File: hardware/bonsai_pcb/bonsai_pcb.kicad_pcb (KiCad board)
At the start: 2 copper layers, 53 x 23 mm, 6 parts, among them J1 Audio Amp Conn, J3 PH2.0 Battery Connector, SW1 BT1, U1 XIAO-ESP32-S3-SMD

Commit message: Update PCB, schematic, and STEP model
Co-Authored-By: Claude Sonnet 5 <noreply@anthropic.com>
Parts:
- removed J1: Audio Amp Conn, Connector_PinSocket_2.54mm:PinSocket_1x07_P2.54mm_Vertical
- removed J3: PH2.0 Battery Connector, Connector_JST:JST_PH_S2B-PH-K_1x02_P2.00mm_Horizontal
- added +: Conn_01x01_Socket, Connector_Wire:SolderWirePad_1x01_SMD_2x4mm, F.Cu at (135.7, 99.0)
- added -: Conn_01x01_Socket, Connector_Wire:SolderWirePad_1x01_SMD_2x4mm, F.Cu at (135.7, 95.2)
- added C1: 10uF, JLCPCB_Capacitors:C0402, F.Cu at (143.0, 100.0)
- added C2: 100nF, JLCPCB_Capacitors:C0402, F.Cu at (143.0, 99.0)
- added CN2: S2B-PH-SM4-TB, JLCPCB_Connectors:CONN-SMD_P2.00_S2B-PH-SM4-TB-LF-SN, F.Cu at (168.8, 104.6)
- added M2: MountingHole_2.2mm_M2, MountingHole:MountingHole_2.2mm_M2, F.Cu at (170.9, 97.7)
- added U2: MAX98357AETE+T, JLCPCB_Amplifiers:TQFN-16_L3.0-W3.0-P0.50-BL-EP1.5, F.Cu at (141.8, 96.3)
- SW1: value BT1 -> TS-1102N-5516; footprint Button_Switch_THT:SW_PUSH_6mm -> JLCPCB_Switches:SW-TH_TS-1102N-5516
- moved SW1 30.2 mm to (138.0, 89.2), turned to 180 degrees
- moved J2 4.01 mm to (163.8, 104.7), turned to -155 degrees
- moved G*** 3.60 mm to (138.6, 94.1)
- renumbered B+ to J2
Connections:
- U1 pad 1: BT1 -> DIN
- U1 pad 10: BLCK -> SD
- U1 pad 2: unconnected-(U1-GPIO2_A1_D1-Pad2) -> BLCK
- U1 pad 3: unconnected-(U1-GPIO3_A2_D2-Pad3) -> LRC
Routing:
- net BLCK: track 28.7 -> 7.57 mm
- net LRC: track 25.8 -> 5.90 mm
- net BT1: track 21.5 -> 36.4 mm
- net /OUTP: track 0.00 -> 12.3 mm, vias 0 -> 2
- net /OUTN: track 0.00 -> 11.5 mm, vias 0 -> 2
- net DIN: track 0.00 -> 10.7 mm
- net GND: track 2.58 -> 12.1 mm, vias 17 -> 21
- net SD: track 37.0 -> 29.7 mm
- net Net-(J2-Pin_1): track 16.9 -> 9.70 mm, vias 0 -> 1
- net VIN: track 33.0 -> 31.1 mm
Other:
- board size 53 x 23 mm -> 41 x 23 mm
- board text removed: "⌈ ⌉ MAX98357 ⌊ ⌋"

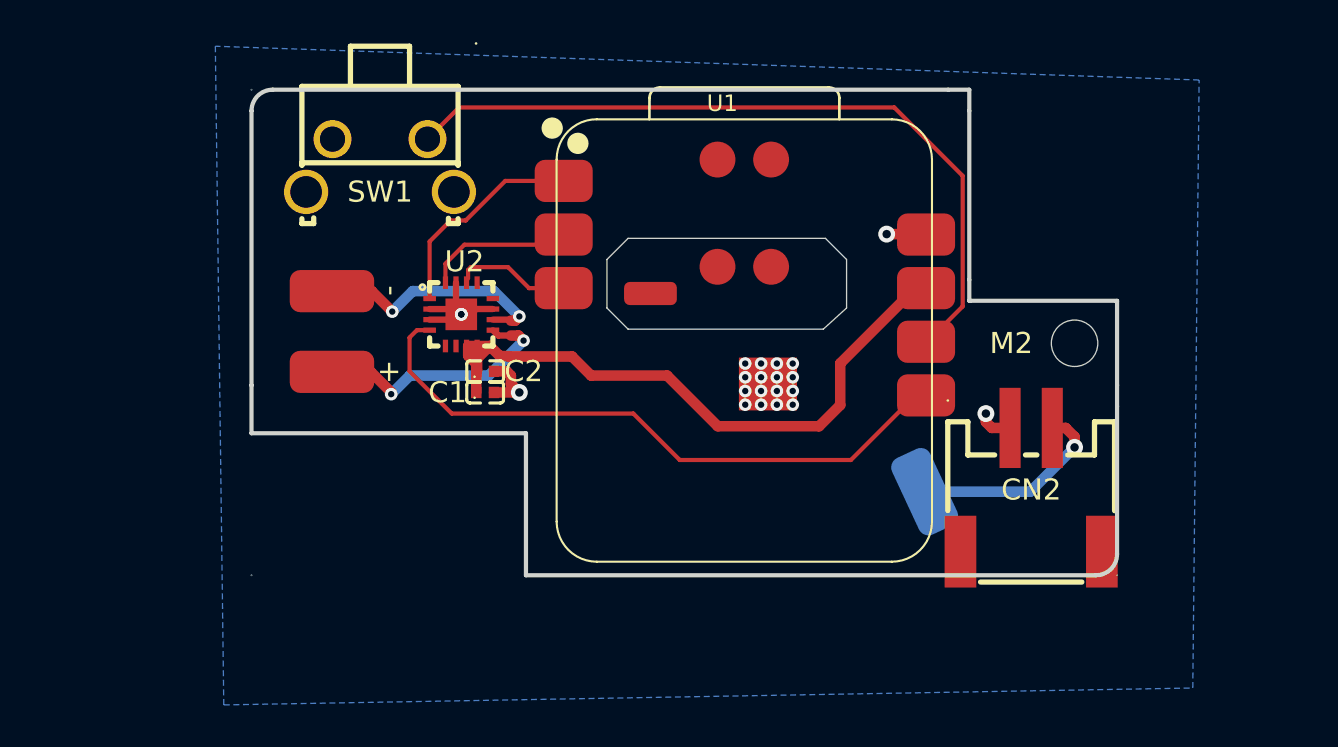
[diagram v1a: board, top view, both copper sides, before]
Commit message: Redraw the board with the tactile switch and the logo silkscreen
Brings in the JLCPCB tactile-switch symbol/footprint/3D model, adds the
logo footprint on the silkscreen, and reworks the schematic and layout
around them.

Co-Authored-By: Claude Opus 5 <noreply@anthropic.com>
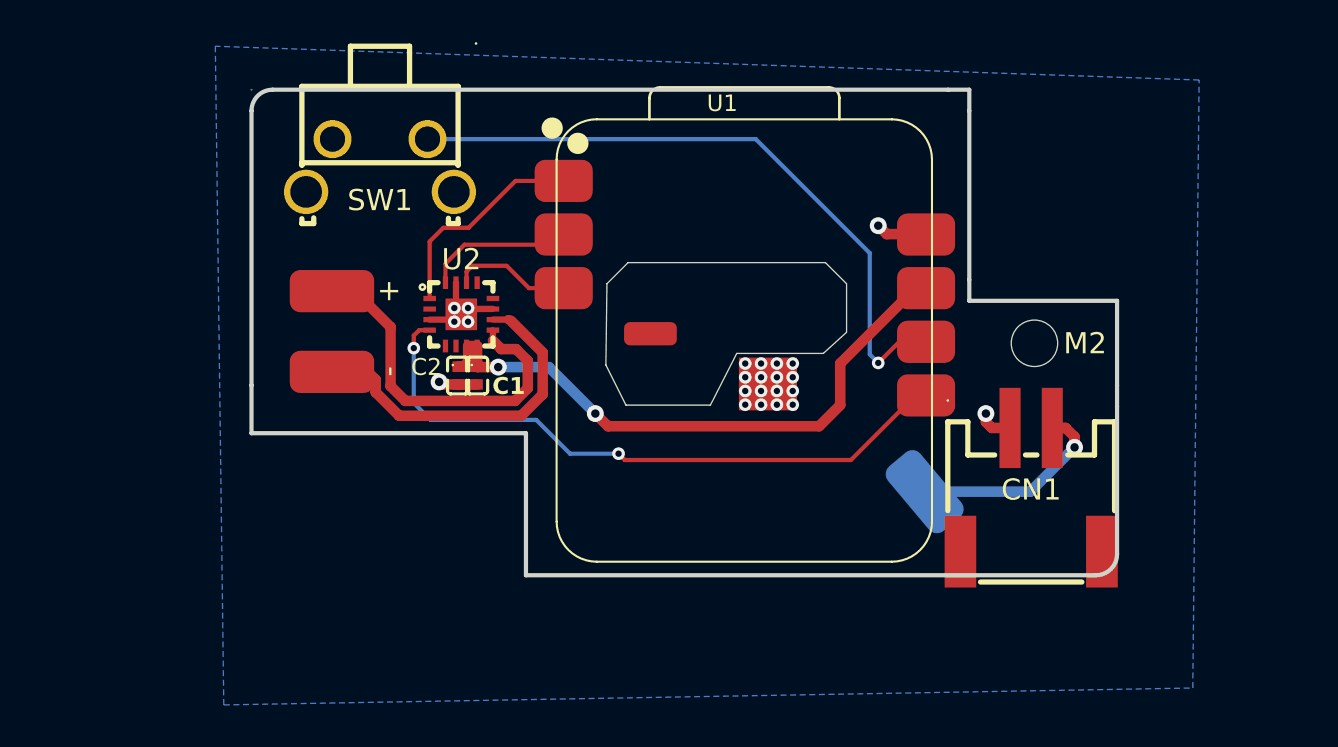
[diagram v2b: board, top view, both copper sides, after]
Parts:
- removed the G*** at (138.6, 94.1)
- added G***: LOGO, LOGO, B.Cu at (140.0, 94.0)
- J1: renamed from J2; value B+ Wire -> B+ Solder Pad
- moved + 3.83 mm to (135.7, 95.2)
- moved - 3.83 mm to (135.7, 99.0)
- moved M2 1.90 mm to (169.0, 97.7)
- moved C2 1.30 mm to (141.7, 99.2), turned to -90 degrees
- moved C1 0.89 mm to (142.6, 99.2), turned to -90 degrees
- turned J1 to 40 degrees
- renumbered CN2 to CN1
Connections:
- net Net-(J2-Pin_1) renamed /BAT +
- U2 pad 2: GND -> unconnected-(U2-GAIN_SLOT-Pad2)
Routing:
- net BT1: track 36.4 -> 30.7 mm, vias 0 -> 1
- net /OUTN: track 11.5 -> 16.7 mm, vias 2 -> 0
- net /OUTP: track 12.3 -> 17.2 mm, vias 2 -> 0
- net GND: track 12.1 -> 9.15 mm, vias 21 -> 23
- net VIN: track 31.1 -> 29.4 mm, vias 0 -> 2
- net SD: track 29.7 -> 30.2 mm, vias 0 -> 2
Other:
- outline, holes or cut-outs redrawn
- board text added: "v0.2 ${CURRENT_DATE} Biel Vázquez Mata"
- board text removed: "->"
- board text removed: "v0.1 23/07/26 Biel Vazquez Mata"
